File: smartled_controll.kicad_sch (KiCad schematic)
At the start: 96 parts, among them J1 Conn_01x04, J2 Conn_01x02, SW1 SW_Push, U1 OC5028B, U2 MAX485E, U3 PY32F003F1xUx, U4 OC5864, U5 need chooice, U6 OC5028B, U7 need chooice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

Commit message: 按照数据手册将PY32中心焊盘接GND
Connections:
- net GND: now also U3.21 (EP)
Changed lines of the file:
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@@
 	)
 	(junction
+		(at 95.25 106.68)
+		(diameter 0)
+		(color 0 0 0 0)
+	)
+	(junction
 		(at 254 85.09)
 		(diameter 0)
@@
 	(wire
 		(pts
+			(xy 95.25 106.68) (xy 97.79 106.68)
+		)
+		(stroke
+			(width 0)
+			(type default)
+		)
+	)
+	(wire
+		(pts
 			(xy 193.04 52.07) (xy 179.07 52.07)
 		)
@@
 		(pin "19"
 		)
+		(pin "21"
+		)
 		(instances

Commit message: 按OC5028B数据手册将第二脚NC改成不连接
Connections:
- net GND: no longer U1.2 (NC), U6.2 (NC), U8.2 (NC), U9.2 (NC)

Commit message: 在RS485的两条差分线间再添加一个气体放电管，都改为1206封装
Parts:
- added GD3: GDT_2Pin, Capacitor_SMD:C_1206_3216Metric, symbol Device:GDT_3Pin
- GD1, GD2: footprint Capacitor_SMD:C_1812_4532Metric -> Capacitor_SMD:C_1206_3216Metric
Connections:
- net 485+: now also GD3.1
- net 485-: now also GD3.2
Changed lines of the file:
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@@
 	)
 	(junction
+		(at 254 93.98)
+		(diameter 0)
+		(color 0 0 0 0)
+	)
+	(junction
 		(at 203.2 80.01)
 		(diameter 0)
@@
 	)
 	(junction
+		(at 246.38 88.9)
+		(diameter 0)
+		(color 0 0 0 0)
+	)
+	(junction
 		(at 90.17 144.78)
 		(diameter 0)
@@
 	(wire
 		(pts
+			(xy 246.38 88.9) (xy 246.38 93.98)
+		)
+		(stroke
+			(width 0)
+			(type default)
+		)
+	)
+	(wire
+		(pts
 			(xy 48.26 144.78) (xy 48.26 147.32)
 		)
@@
 	(wire
 		(pts
-			(xy 246.38 80.01) (xy 246.38 93.98)
+			(xy 246.38 80.01) (xy 246.38 88.9)
 		)
 		(stroke
@@
 	(wire
 		(pts
+			(xy 251.46 93.98) (xy 254 93.98)
+		)
+		(stroke
+			(width 0)
+			(type default)
+		)
+	)
+	(wire
+		(pts
 			(xy 81.28 99.06) (xy 82.55 99.06)
 		)
@@
 	)
 	(symbol
+		(lib_id "Device:GDT_3Pin")
+		(at 251.46 88.9 270)
+		(mirror x)
+		(unit 1)
+		(exclude_from_sim no)
+		(in_bom yes)
+		(on_board yes)
+		(dnp no)
+		(property "Reference" "GD3"
+			(at 252.7301 83.82 0)
+			(effects
+				(font
+					(size 1.27 1.27)
+				)
+				(justify left)
+			)
+		)
+		(property "Value" "GDT_2Pin"
+			(at 250.1901 83.82 0)
+			(effects
+				(font
+					(size 1.27 1.27)
+				)
+				(justify left)
+			)
+		)
+		(property "Footprint" "Capacitor_SMD:C_1206_3216Metric"
+			(at 251.46 88.9 90)
+			(effects
+				(font
+					(size 1.27 1.27)
+				)
+				(hide yes)
+			)
+		)
+		(property "Datasheet" "~"
+			(at 251.46 88.9 90)
+			(effects
+				(font
+					(size 1.27 1.27)
+				)
+				(hide yes)
+			)
+		)
+		(property "Description" "Gas Discharge Tube with 3 Pins"
+			(at 251.46 88.9 0)
+			(effects
+				(font
+					(size 1.27 1.27)
+				)
+				(hide yes)
+			)
+		)
+		(pin "1"
+		)
+		(pin "3"
+		)
+		(pin "2"
+		)
+		(instances
+			(project "smartled_controll"
+				(path "/b299fa7e-4ddc-4ca9-9929-510e6cf892c6"
+					(reference "GD3")
+					(unit 1)
+				)
+			)
+		)
+	)
+	(symbol
 		(lib_id "Device:D_Schottky")
 		(at 195.58 45.72 270)
@@
 			)
 		)
-		(property "Footprint" "Capacitor_SMD:C_1812_4532Metric"
+		(property "Footprint" "Capacitor_SMD:C_1206_3216Metric"
 			(at 246.38 99.06 90)
 			(effects
@@
 			)
 		)
-		(property "Footprint" "Capacitor_SMD:C_1812_4532Metric"
+		(property "Footprint" "Capacitor_SMD:C_1206_3216Metric"
 			(at 254 99.06 90)
 			(effects

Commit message: 保险丝改成2410(6125)封装
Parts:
- F3: footprint Fuse:Fuse_1206_3216Metric -> project_footprints:Fuse_2410_6125Metric
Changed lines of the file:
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@@
 			)
 		)
-		(property "Footprint" "Fuse:Fuse_1206_3216Metric"
+		(property "Footprint" "project_footprints:Fuse_2410_6125Metric"
 			(at 68.58 30.988 90)
 			(effects

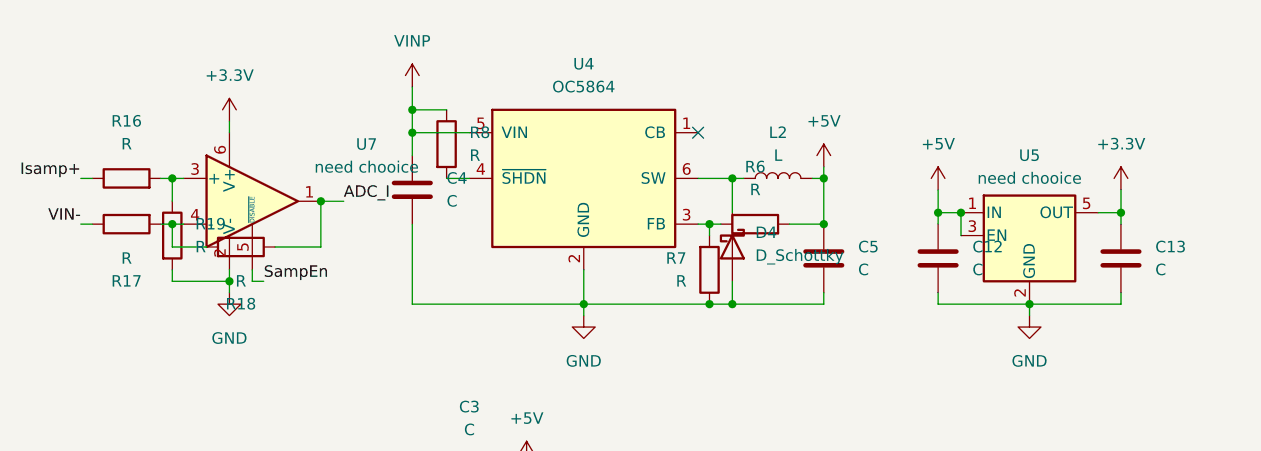
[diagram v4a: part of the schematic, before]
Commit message: 选择3.3V LDO和电流采样运放的型号
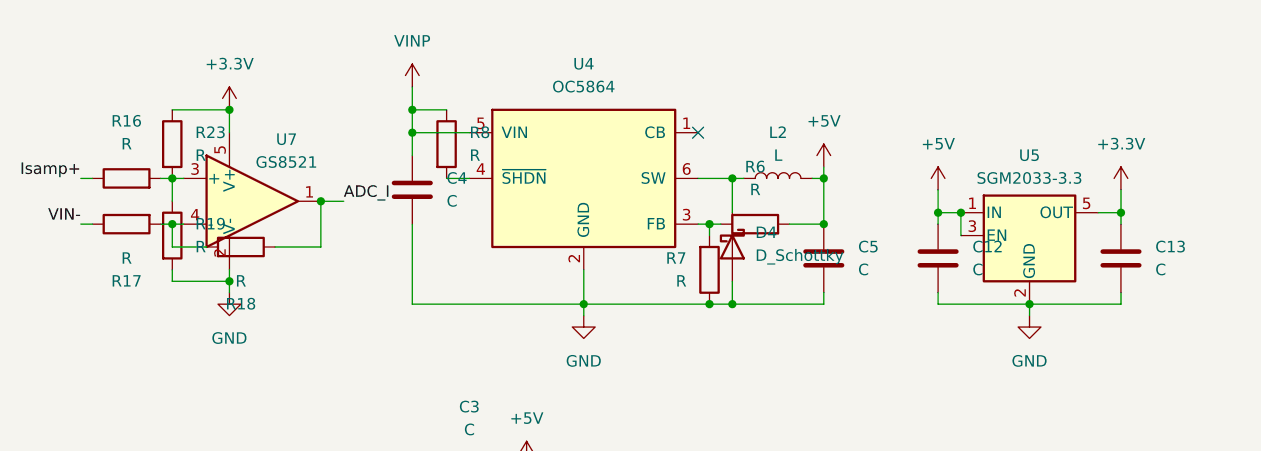
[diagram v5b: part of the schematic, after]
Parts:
- added R23: R, Resistor_SMD:R_0402_1005Metric, symbol Device:R
- U5: value need chooice -> SGM2033-3.3
- U7: value need chooice -> GS8521; footprint Package_TO_SOT_SMD:SOT-23-6 -> Package_TO_SOT_SMD:TSOT-23-5; symbol Amplifier_Operational:ADA4807-1 -> Amplifier_Operational:AD8603
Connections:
- net +3.3V: now also U7.5 (V+), R23.1; no longer U7.6 (V+)
- net SampEn: no longer U7.5 (~{DISABLE})
- net at R16.2, R19.1, U7.3 (+): now also R23.2
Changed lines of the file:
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@@
 	)
 	(junction
+		(at 139.7 30.48)
+		(diameter 0)
+		(color 0 0 0 0)
+	)
+	(junction
 		(at 133.35 38.1)
 		(diameter 0)
@@
 	(wire
 		(pts
-			(xy 143.51 49.53) (xy 142.24 49.53)
-		)
-		(stroke
-			(width 0)
-			(type default)
-		)
-	)
-	(wire
-		(pts
 			(xy 68.58 185.42) (xy 69.85 185.42)
 		)
@@
 	(wire
 		(pts
-			(xy 139.7 31.75) (xy 139.7 33.02)
+			(xy 139.7 30.48) (xy 139.7 33.02)
 		)
 		(stroke
@@
 	(wire
 		(pts
-			(xy 142.24 49.53) (xy 142.24 48.26)
-		)
-		(stroke
-			(width 0)
-			(type default)
-		)
-	)
-	(wire
-		(pts
 			(xy 55.88 59.69) (xy 55.88 57.15)
 		)
@@
 	(wire
 		(pts
+			(xy 133.35 30.48) (xy 139.7 30.48)
+		)
+		(stroke
+			(width 0)
+			(type default)
+		)
+	)
+	(wire
+		(pts
 			(xy 81.28 81.28) (xy 82.55 81.28)
 		)
@@
 		)
 	)
-	(label "SampEn"
-		(at 143.51 49.53 0)
-		(effects
-			(font
-				(size 1.27 1.27)
-			)
-			(justify left bottom)
-		)
-	)
 	(label "VIN+"
 		(at 22.86 34.29 180)
@@
 	(symbol
 		(lib_id "power:+3.3V")
-		(at 139.7 31.75 0)
+		(at 139.7 30.48 0)
 		(unit 1)
 		(exclude_from_sim no)
@@
 		(fields_autoplaced yes)
 		(property "Reference" "#PWR26"
-			(at 139.7 35.56 0)
+			(at 139.7 34.29 0)
 			(effects
 				(font
@@
 		)
 		(property "Value" "+3.3V"
-			(at 139.7 26.67 0)
+			(at 139.7 25.4 0)
 			(effects
 				(font
@@
 		)
 		(property "Footprint" ""
-			(at 139.7 31.75 0)
+			(at 139.7 30.48 0)
 			(effects
 				(font
@@
 		)
 		(property "Datasheet" ""
-			(at 139.7 31.75 0)
+			(at 139.7 30.48 0)
 			(effects
 				(font
@@
 		)
 		(property "Description" "Power symbol creates a global label with name \"+3.3V\""
-			(at 139.7 31.75 0)
+			(at 139.7 30.48 0)
 			(effects
 				(font
@@
 	)
 	(symbol
+		(lib_id "Device:R")
+		(at 133.35 34.29 0)
+		(unit 1)
+		(exclude_from_sim no)
+		(in_bom yes)
+		(on_board yes)
+		(dnp no)
+		(property "Reference" "R23"
+			(at 135.89 33.0199 0)
+			(effects
+				(font
+					(size 1.27 1.27)
+				)
+				(justify left)
+			)
+		)
+		(property "Value" "R"
+			(at 135.89 35.5599 0)
+			(effects
+				(font
+					(size 1.27 1.27)
+				)
+				(justify left)
+			)
+		)
+		(property "Footprint" "Resistor_SMD:R_0402_1005Metric"
+			(at 131.572 34.29 90)
+			(effects
+				(font
+					(size 1.27 1.27)
+				)
+				(hide yes)
+			)
+		)
+		(property "Datasheet" "~"
+			(at 133.35 34.29 0)
+			(effects
+				(font
+					(size 1.27 1.27)
+				)
+				(hide yes)
+			)
+		)
+		(property "Description" "Resistor"
+			(at 133.35 34.29 0)
+			(effects
+				(font
+					(size 1.27 1.27)
+				)
+				(hide yes)
+			)
+		)
+		(pin "1"
+		)
+		(pin "2"
+		)
+		(instances
+			(project "smartled_controll"
+				(path "/b299fa7e-4ddc-4ca9-9929-510e6cf892c6"
+					(reference "R23")
+					(unit 1)
+				)
+			)
+		)
+	)
+	(symbol
 		(lib_id "power:GND")
 		(at 144.78 147.32 0)
@@
 			)
 		)
-		(property "Value" "need chooice"
+		(property "Value" "SGM2033-3.3"
 			(at 228.6 38.1 0)
 			(effects
@@
 	)
 	(symbol
-		(lib_id "Amplifier_Operational:ADA4807-1")
+		(lib_id "Amplifier_Operational:AD8603")
 		(at 142.24 40.64 0)
 		(unit 1)
@@
 		(on_board yes)
 		(dnp no)
-		(fields_autoplaced yes)
 		(property "Reference" "U7"
-			(at 154.94 34.3214 0)
+			(at 146.05 33.782 0)
 			(effects
 				(font
@@
 			)
 		)
-		(property "Value" "need chooice"
-			(at 154.94 36.8614 0)
+		(property "Value" "GS8521"
+			(at 146.05 36.322 0)
 			(effects
 				(font
@@
 			)
 		)
-		(property "Footprint" "Package_TO_SOT_SMD:SOT-23-6"
-			(at 142.24 46.99 0)
+		(property "Footprint" "Package_TO_SOT_SMD:TSOT-23-5"
+			(at 142.24 40.64 0)
 			(effects
 				(font
@@
 			)
 		)
-		(property "Datasheet" ""
-			(at 142.24 49.53 0)
+		(property "Datasheet" "http://www.gainsil.com/images/product/65_2.pdf"
+			(at 142.24 35.56 0)
 			(effects
 				(font
 					(size 1.27 1.27)
 				)
-				(justify left)
 				(hide yes)
 			)
 		)
-		(property "Description" "Single Rail-to-Rail Input/Output Amplifiers, with disable, SC-70-6/SOT-23-6"
+		(property "Description" "Precision Micropower, Low Noise CMOS, Rail-to-Rail Input/Output Operational Amplifier, TSOT-23-5"
 			(at 142.24 40.64 0)
 			(effects
@@
 		(pin "4"
 		)
-		(pin "6"
-		)
 		(pin "2"

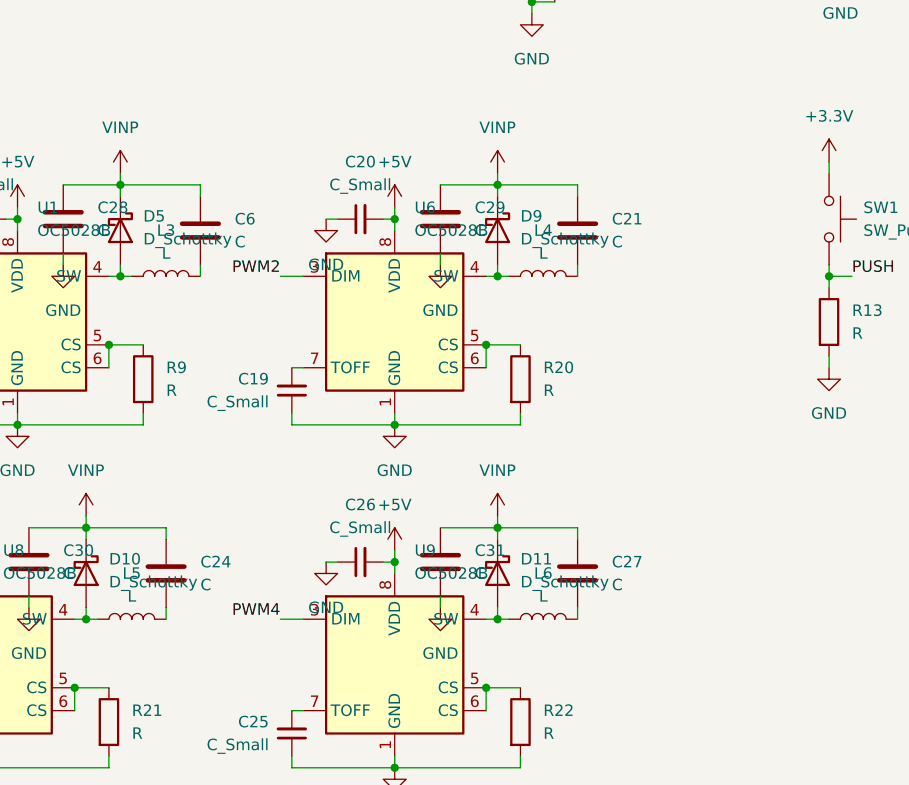
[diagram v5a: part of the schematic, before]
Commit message: 添加LED接口焊盘
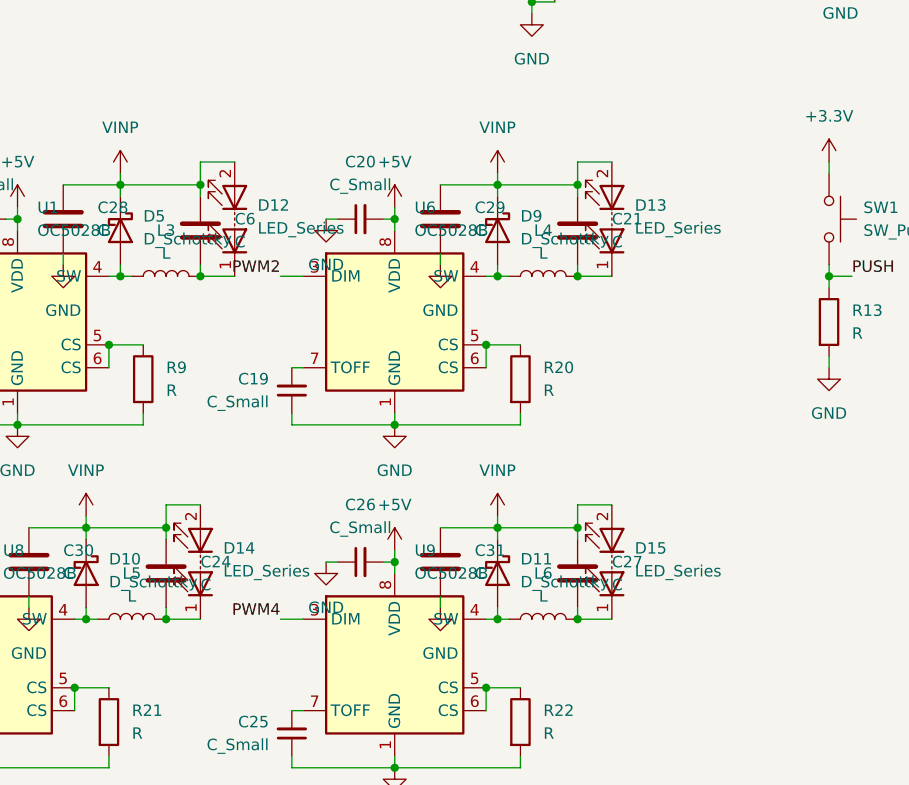
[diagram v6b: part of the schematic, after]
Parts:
- added D12, D13, D14, D15: LED_Series, project_footprints:2Pads_1.0x1.5mm_P2.0mm_mpsign, symbol Device:LED_Series
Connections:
- net VINP: now also D12.2 (A), D13.2 (A), D14.2 (A), D15.2 (A)
- net at C6.2, L3.2: now also D12.1 (K)
- net at C27.2, L6.2: now also D15.1 (K)
- net at C24.2, L5.2: now also D14.1 (K)
- net at C21.2, L4.2: now also D13.1 (K)
